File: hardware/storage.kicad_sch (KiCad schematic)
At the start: 9 parts, among them J6 Micro_SD_Card_Det1, U21 EMMC5.1_BGA153

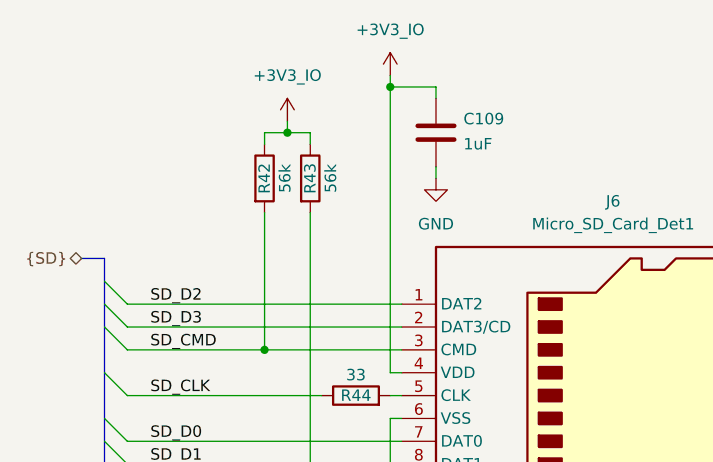
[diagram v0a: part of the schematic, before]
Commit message: Improve routing and add test pads
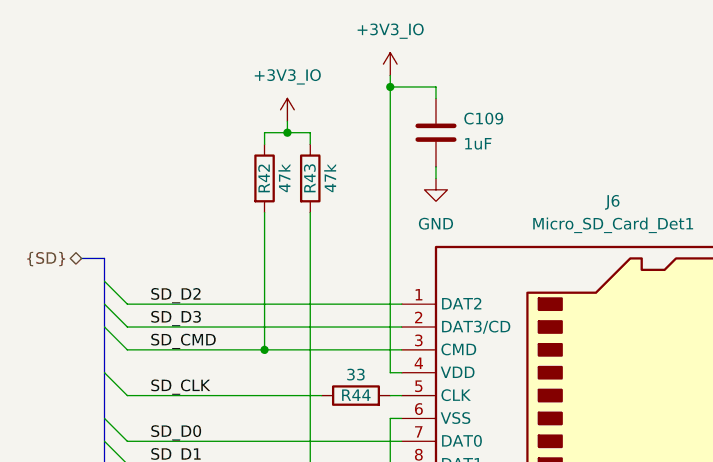
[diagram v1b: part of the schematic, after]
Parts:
- J6: FT Position Offset -1.905,0 -> 0,0.381
- R42, R43: value 56k -> 47k; LCSC Part # C25796 -> C25792
- U21: LCSC Part # C5821038 -> C2830403
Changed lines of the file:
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@@
 			)
 		)
-		(property "Value" "56k"
+		(property "Value" "47k"
 			(at 84.836 74.93 90)
 			(effects
@@
 			)
 		)
-		(property "LCSC Part #" "C25796"
+		(property "LCSC Part #" "C25792"
 			(at 82.55 74.93 90)
 			(effects
@@
 			)
 		)
-		(property "FT Position Offset" "-1.905,0"
+		(property "FT Position Offset" "0,0.381"
 			(at 120.65 99.06 0)
 			(effects
@@
 			)
 		)
-		(property "Value" "56k"
+		(property "Value" "47k"
 			(at 89.916 74.93 90)
 			(effects
@@
 			)
 		)
-		(property "LCSC Part #" "C25796"
+		(property "LCSC Part #" "C25792"
 			(at 87.63 74.93 90)
 			(effects
@@
 			)
 		)
-		(property "LCSC Part #" "C5821038"
+		(property "LCSC Part #" "C2830403"
 			(at 196.85 96.52 0)
 			(effects

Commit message: Production ready
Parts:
- R42, R43: value 47k -> 56k; LCSC Part # C25792 -> C25796
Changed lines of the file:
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@@
 			)
 		)
-		(property "Value" "47k"
+		(property "Value" "56k"
 			(at 84.836 74.93 90)
 			(effects
@@
 			)
 		)
-		(property "LCSC Part #" "C25792"
+		(property "LCSC Part #" "C25796"
 			(at 82.55 74.93 90)
 			(effects
@@
 			)
 		)
-		(property "Value" "47k"
+		(property "Value" "56k"
 			(at 89.916 74.93 90)
 			(effects
@@
 			)
 		)
-		(property "LCSC Part #" "C25792"
+		(property "LCSC Part #" "C25796"
 			(at 87.63 74.93 90)
 			(effects
